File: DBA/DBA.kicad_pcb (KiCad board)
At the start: 2 copper layers, 45.7 x 61 mm, 1 part, among them U1 ESP32_NodeMCU_v1.1

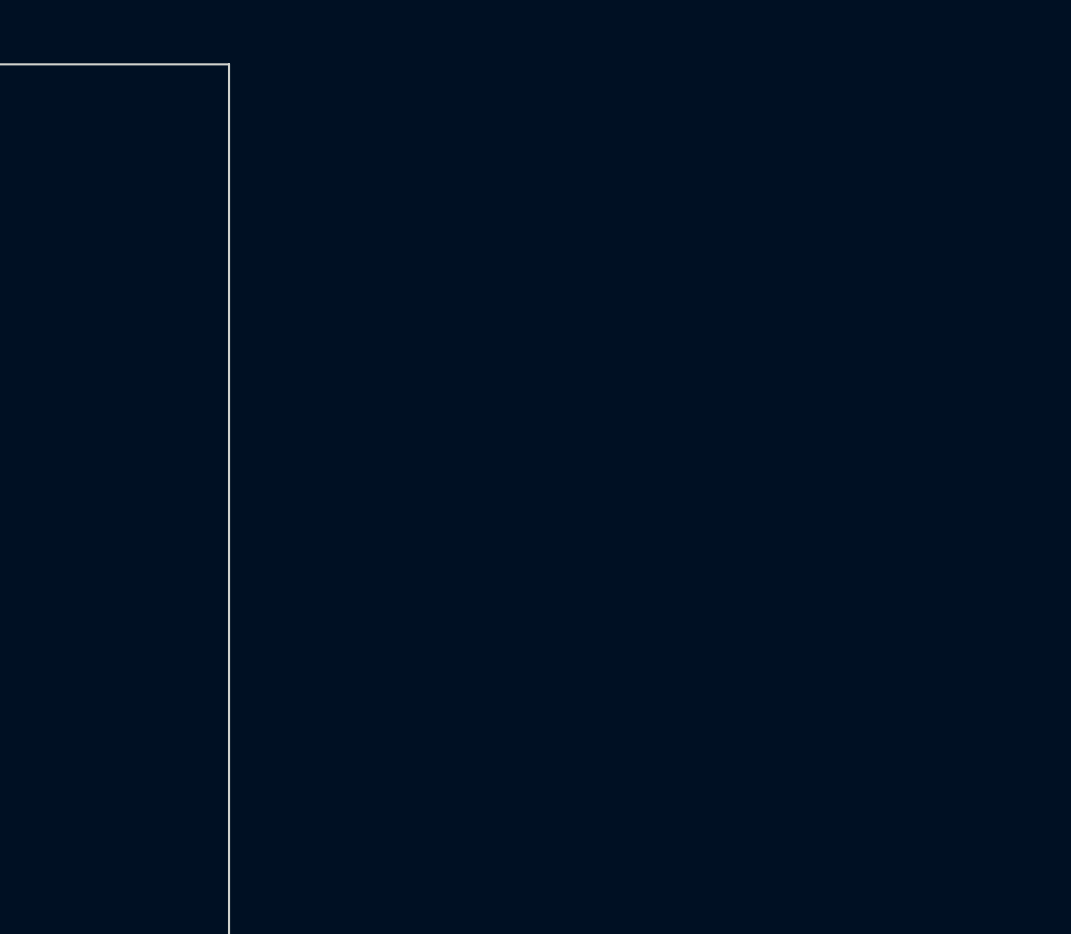
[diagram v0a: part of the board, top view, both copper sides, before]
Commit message: Created symbols for primary and secondary microphone
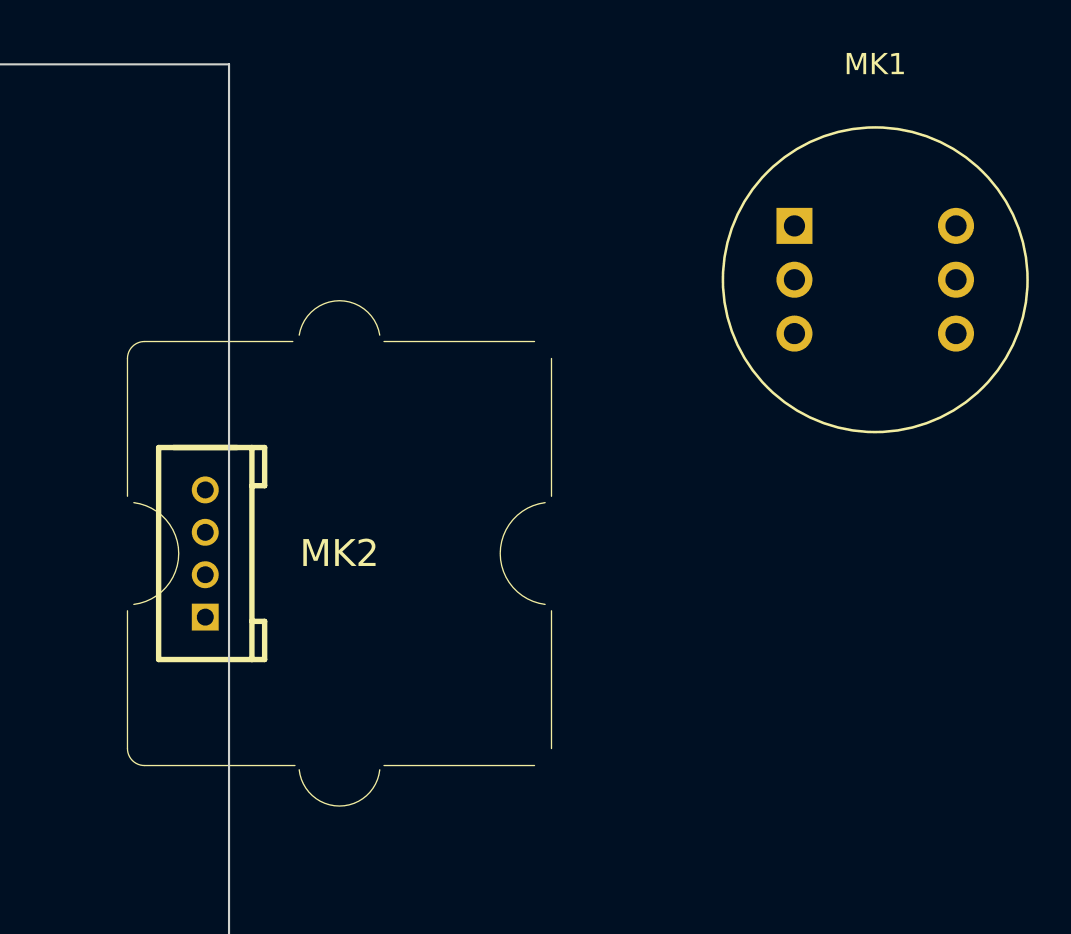
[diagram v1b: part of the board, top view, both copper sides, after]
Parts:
- added MK1: INMP441, Microphones:INMP441, F.Cu at (195.6, 71.1)
- added MK2: Grove, Microphones:Grove Sound Sensor, F.Cu at (170.3, 84.0)
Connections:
- U1 pad 1: unconnected-(U1-Pad1) -> Net-(MK1-Pad5)
- U1 pad 10: unconnected-(U1-Pad10) -> Net-(MK1-Pad4)
- U1 pad 14: unconnected-(U1-Pad14) -> GND
- U1 pad 32: unconnected-(U1-Pad32) -> GND
- U1 pad 36: unconnected-(U1-Pad36) -> Net-(MK1-Pad3)
- U1 pad 37: unconnected-(U1-Pad37) -> Net-(MK1-Pad2)
- U1 pad 38: unconnected-(U1-Pad38) -> GND
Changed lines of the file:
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@@
   (net 2 "unconnected-(U1-Pad8)")
   (net 3 "unconnected-(U1-Pad9)")
-  (net 4 "unconnected-(U1-Pad10)")
+  (net 4 "GND")
   (net 5 "unconnected-(U1-Pad11)")
   (net 6 "unconnected-(U1-Pad12)")
   (net 7 "unconnected-(U1-Pad13)")
-  (net 8 "unconnected-(U1-Pad14)")
+  (net 8 "Net-(MK1-Pad2)")
   (net 9 "unconnected-(U1-Pad15)")
   (net 10 "unconnected-(U1-Pad16)")
@@
   (net 22 "unconnected-(U1-Pad30)")
   (net 23 "unconnected-(U1-Pad31)")
-  (net 24 "unconnected-(U1-Pad32)")
+  (net 24 "Net-(MK1-Pad3)")
   (net 25 "unconnected-(U1-Pad33)")
   (net 26 "unconnected-(U1-Pad34)")
   (net 27 "unconnected-(U1-Pad35)")
-  (net 28 "unconnected-(U1-Pad36)")
-  (net 29 "unconnected-(U1-Pad38)")
-  (net 30 "unconnected-(U1-Pad1)")
+  (net 28 "Net-(MK1-Pad4)")
+  (net 29 "Net-(MK1-Pad5)")
+  (net 30 "unconnected-(MK2-Pad3)")
   (net 31 "unconnected-(U1-Pad2)")
   (net 32 "unconnected-(U1-Pad3)")
@@
   (net 36 "unconnected-(U1-Pad19)")
   (net 37 "unconnected-(U1-Pad26)")
-  (net 38 "unconnected-(U1-Pad37)")
+  (net 38 "unconnected-(MK2-Pad4)")
+  (footprint "Microphones:INMP441" (layer "F.Cu")
+    (at 195.58 71.12)
+    (descr "Through hole straight pin header, 2x03, 2.54mm pitch, double rows")
+    (tags "Through hole pin header THT 2x03 2.54mm double row")
+    (property "Sheetfile" "DBA.kicad_sch")
+    (property "Sheetname" "")
+    (attr through_hole)
+    (fp_text reference "MK1" (at 0 -10.16) (layer "F.SilkS")
+      (effects (font (size 1 1) (thickness 0.15)))
+    )
+    (fp_text value "INMP441" (at 1.27 4.87) (layer "F.Fab")
+      (effects (font (size 1 1) (thickness 0.15)))
+    )
+    (fp_text user "${REFERENCE}" (at -2.54 0 90) (layer "F.Fab")
+      (effects (font (size 1 1) (thickness 0.15)))
+    )
+    (fp_circle (center 0 0) (end 5.08 5.08) (layer "F.SilkS") (width 0.12) (fill none))
+    (fp_circle (center 0 0) (end 7.62 5.08) (layer "F.CrtYd") (width 0.05) (fill none))
+    (pad "1" thru_hole rect (at -3.81 -2.54) (size 1.7 1.7) (drill 1) (layers *.Cu *.Mask)
+      (net 4 "GND") (pinfunction "L/R") (pintype "input"))
+    (pad "2" thru_hole oval (at -3.81 0) (size 1.7 1.7) (drill 1) (layers *.Cu *.Mask)
+      (net 8 "Net-(MK1-Pad2)") (pinfunction "WS") (pintype "input"))
+    (pad "3" thru_hole oval (at -3.81 2.54) (size 1.7 1.7) (drill 1) (layers *.Cu *.Mask)
+      (net 24 "Net-(MK1-Pad3)") (pinfunction "SCK") (pintype "input"))
+    (pad "4" thru_hole oval (at 3.81 2.54) (size 1.7 1.7) (drill 1) (layers *.Cu *.Mask)
+      (net 28 "Net-(MK1-Pad4)") (pinfunction "SD") (pintype "input"))
+    (pad "5" thru_hole oval (at 3.81 0) (size 1.7 1.7) (drill 1) (layers *.Cu *.Mask)
+      (net 29 "Net-(MK1-Pad5)") (pinfunction "VDD") (pintype "power_in"))
+    (pad "6" thru_hole oval (at 3.81 -2.54) (size 1.7 1.7) (drill 1) (layers *.Cu *.Mask)
+      (net 4 "GND") (pinfunction "GND") (pintype "power_in"))
+    (model "${KICAD6_3DMODEL_DIR}/Connector_PinHeader_2.54mm.3dshapes/PinHeader_2x03_P2.54mm_Vertical.wrl"
+      (offset (xyz 0 0 0))
+      (scale (xyz 1 1 1))
+      (rotate (xyz 0 0 0))
+    )
+  )
   (footprint "Package_DIP:DIP-38_W22.86mm" (layer "F.Cu")
     (at 142.24 88.9)
@@
     (fp_line (start 10.485 -22.8) (end 10.485 26.73) (layer "F.Fab") (width 0.1))
     (pad "1" thru_hole rect (at -12.12 -21.53) (size 1.6 1.6) (drill 0.8) (layers *.Cu *.Mask)
-      (net 30 "unconnected-(U1-Pad1)") (pinfunction "3v3") (pintype "power_out"))
+      (net 29 "Net-(MK1-Pad5)") (pinfunction "3v3") (pintype "power_out"))
     (pad "2" thru_hole oval (at -12.12 -18.99) (size 1.6 1.6) (drill 0.8) (layers *.Cu *.Mask)
       (net 31 "unconnected-(U1-Pad2)") (pinfunction "En") (pintype "input"))
@@
       (net 3 "unconnected-(U1-Pad9)") (pinfunction "IO25") (pintype "input"))
     (pad "10" thru_hole oval (at -12.12 1.33) (size 1.6 1.6) (drill 0.8) (layers *.Cu *.Mask)
-      (net 4 "unconnected-(U1-Pad10)") (pinfunction "IO26") (pintype "input"))
+      (net 28 "Net-(MK1-Pad4)") (pinfunction "IO26") (pintype "input"))
     (pad "11" thru_hole oval (at -12.12 3.87) (size 1.6 1.6) (drill 0.8) (layers *.Cu *.Mask)
       (net 5 "unconnected-(U1-Pad11)") (pinfunction "IO27") (pintype "input"))
@@
       (net 7 "unconnected-(U1-Pad13)") (pinfunction "IO12") (pintype "input"))
     (pad "14" thru_hole oval (at -12.12 11.49) (size 1.6 1.6) (drill 0.8) (layers *.Cu *.Mask)
-      (net 8 "unconnected-(U1-Pad14)") (pinfunction "GND") (pintype "power_in"))
+      (net 4 "GND") (pinfunction "GND") (pintype "power_in"))
     (pad "15" thru_hole oval (at -12.12 14.03) (size 1.6 1.6) (drill 0.8) (layers *.Cu *.Mask)
       (net 9 "unconnected-(U1-Pad15)") (pinfunction "IO13") (pintype "input"))
@@
       (net 23 "unconnected-(U1-Pad31)") (pinfunction "IO19") (pintype "input"))
     (pad "32" thru_hole oval (at 10.74 -6.29) (size 1.6 1.6) (drill 0.8) (layers *.Cu *.Mask)
-      (net 24 "unconnected-(U1-Pad32)") (pinfunction "GND") (pintype "power_in"))
+      (net 4 "GND") (pinfunction "GND") (pintype "power_in"))
     (pad "33" thru_hole oval (at 10.74 -8.83) (size 1.6 1.6) (drill 0.8) (layers *.Cu *.Mask)
       (net 25 "unconnected-(U1-Pad33)") (pinfunction "IO21") (pintype "input"))
@@
       (net 27 "unconnected-(U1-Pad35)") (pinfunction "TxD0") (pintype "input"))
     (pad "36" thru_hole oval (at 10.74 -16.45) (size 1.6 1.6) (drill 0.8) (layers *.Cu *.Mask)
-      (net 28 "unconnected-(U1-Pad36)") (pinfunction "IO22") (pintype "input"))
+      (net 24 "Net-(MK1-Pad3)") (pinfunction "IO22") (pintype "input"))
     (pad "37" thru_hole oval (at 10.74 -18.99) (size 1.6 1.6) (drill 0.8) (layers *.Cu *.Mask)
-      (net 38 "unconnected-(U1-Pad37)") (pinfunction "IO23") (pintype "input"))
+      (net 8 "Net-(MK1-Pad2)") (pinfunction "IO23") (pintype "input"))
     (pad "38" thru_hole oval (at 10.74 -21.53) (size 1.6 1.6) (drill 0.8) (layers *.Cu *.Mask)
-      (net 29 "unconnected-(U1-Pad38)") (pinfunction "GND") (pintype "power_in"))
+      (net 4 "GND") (pinfunction "GND") (pintype "power_in"))
     (model "${KICAD6_3DMODEL_DIR}/Package_DIP.3dshapes/DIP-32_W15.24mm.wrl"
       (offset (xyz 0 0 0))
@@
     )
   )
+  (footprint "Microphones:Grove Sound Sensor" (layer "F.Cu")
+    (at 170.3096 84.033788)
+    (property "Sheetfile" "DBA.kicad_sch")
+    (property "Sheetname" "")
+    (fp_text reference "MK2" (at 0 0) (layer "F.SilkS")
+      (effects (font (size 1.27 1.27) (thickness 0.15)))
+    )
+    (fp_text value "Grove" (at 0 0) (layer "F.Fab") hide
+      (effects (font (size 1.27 1.27) (thickness 0.15)))
+    )
+    (fp_line (start -4.13 3.2) (end -4.13 -3.2) (layer "F.SilkS") (width 0.254))
+    (fp_line (start -7.33 5) (end -5.33 5) (layer "F.SilkS") (width 0.127))
+    (fp_line (start -9.2 -10) (end -2.2 -10) (layer "F.SilkS") (width 0.0254))
+    (fp_line (start -3.53 5) (end -3.53 3.2) (layer "F.SilkS") (width 0.254))
+    (fp_line (start -3.53 -3.2) (end -3.53 -5) (layer "F.SilkS") (width 0.254))
+    (fp_line (start -3.53 3.2) (end -4.13 3.2) (layer "F.SilkS") (width 0.254))
+    (fp_line (start -8.53 5) (end -4.13 5) (layer "F.SilkS") (width 0.254))
+    (fp_line (start 10 -2.7) (end 10 -9.2) (layer "F.SilkS") (width 0.0254))
+    (fp_line (start -3.53 -5) (end -4.13 -5) (layer "F.SilkS") (width 0.254))
+    (fp_line (start -9.2 10) (end -2.1 10) (layer "F.SilkS") (width 0.0254))
+    (fp_line (start -4.13 -3.2) (end -3.53 -3.2) (layer "F.SilkS") (width 0.254))
+    (fp_line (start 10 2.7) (end 10 9.2) (layer "F.SilkS") (width 0.0254))
+    (fp_line (start 9.2 -10) (end 2.1 -10) (layer "F.SilkS") (width 0.0254))
+    (fp_line (start -4.13 5) (end -3.53 5) (layer "F.SilkS") (width 0.254))
+    (fp_line (start -4.13 5) (end -4.13 3.2) (layer "F.SilkS") (width 0.254))
+    (fp_line (start -4.13 -3.2) (end -4.13 -5) (layer "F.SilkS") (width 0.254))
+    (fp_line (start -7.83 -5) (end -4.83 -5) (layer "F.SilkS") (width 0.254))
+    (fp_line (start 9.2 10) (end 2.1 10) (layer "F.SilkS") (width 0.0254))
+    (fp_line (start -4.13 -5) (end -8.53 -5) (layer "F.SilkS") (width 0.254))
+    (fp_line (start -8.53 5) (end -8.53 -5) (layer "F.SilkS") (width 0.254))
+    (fp_line (start -10 2.7) (end -10 9.2) (layer "F.SilkS") (width 0.0254))
+    (fp_line (start -10 -2.7) (end -10 -9.2) (layer "F.SilkS") (width 0.0254))
+    (fp_arc (start 1.9 10.2) (mid -0.000001 11.910767) (end -1.9 10.199998) (layer "F.SilkS") (width 0.0254))
+    (fp_arc (start -9.2 10) (mid -9.765685 9.765685) (end -10 9.2) (layer "F.SilkS") (width 0.0254))
+    (fp_arc (start -1.9 -10.3) (mid 0 -11.924188) (end 1.9 -10.3) (layer "F.SilkS") (width 0.0254))
+    (fp_arc (start -9.7 -2.4) (mid -7.582254 0) (end -9.7 2.4) (layer "F.SilkS") (width 0.0254))
+    (fp_arc (start 9.7 2.4) (mid 7.582254 0) (end 9.7 -2.4) (layer "F.SilkS") (width 0.0254))
+    (fp_arc (start -10 -9.2) (mid -9.765685 -9.765685) (end -9.2 -10) (layer "F.SilkS") (width 0.0254))
+    (pad "1" thru_hole rect (at -6.33 3 90) (size 1.27 1.27) (drill 0.8) (layers *.Cu *.Mask)
+      (net 4 "GND") (pinfunction "GND") (pintype "power_in") (solder_mask_margin 0.0508))
+    (pad "2" thru_hole circle (at -6.33 1 90) (size 1.27 1.27) (drill 0.8) (layers *.Cu *.Mask)
+      (net 29 "Net-(MK1-Pad5)") (pinfunction "VCC") (pintype "power_in") (solder_mask_margin 0.0508))
+    (pad "3" thru_hole circle (at -6.33 -1 90) (size 1.27 1.27) (drill 0.8) (layers *.Cu *.Mask)
+      (net 30 "unconnected-(MK2-Pad3)") (pinfunction "NC") (pintype "no_connect") (solder_mask_margin 0.0508))
+    (pad "4" thru_hole circle (at -6.33 -3 90) (size 1.27 1.27) (drill 0.8) (layers *.Cu *.Mask)
+      (net 38 "unconnected-(MK2-Pad4)") (pinfunction "SIG") (pintype "output") (solder_mask_margin 0.0508))
+  )
   (gr_rect (start 165.1 121.92) (end 119.38 60.96) (layer "Edge.Cuts") (width 0.1) (fill none))

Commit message: First complete model
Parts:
- added A1: TP4056, custom:TP4056Board, B.Cu at (119.4, 101.6)
- added BT1: Battery_Cell, Battery:BatteryHolder_Keystone_1042_1x18650, B.Cu at (160.0, 86.4)
- added C1: 100n, Capacitor_THT:C_Radial_D6.3mm_H5.0mm_P2.50mm, F.Cu at (166.4, 108.0)
- added C2: 100u, Capacitor_THT:CP_Radial_D5.0mm_P2.50mm, F.Cu at (157.5, 110.5)
- added J4: Conn_01x01_Male, Connector_PinHeader_2.54mm:PinHeader_1x01_P2.54mm_Vertical, F.Cu at (138.4, 109.2)
- added J5: Conn_01x01_Male, Connector_PinHeader_2.54mm:PinHeader_1x01_P2.54mm_Vertical, F.Cu at (151.1, 102.9)
- added U2: MCP1700-3302E_TO92, Package_TO_SOT_THT:TO-92_Inline, F.Cu at (147.3, 108.0)
- moved MK1 49.3 mm to (147.3, 81.3), turned to 90 degrees
- moved MK2 40.4 mm to (147.3, 50.8), turned to 90 degrees
- moved U1 30.6 mm to (119.4, 68.6), turned to 180 degrees
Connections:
- MK2 pad 4: unconnected-(MK2-Pad4) -> Net-(MK2-Pad4)
- U1 pad 9: unconnected-(U1-Pad9) -> Net-(MK2-Pad4)
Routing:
- net Net-(C1-Pad2): track 0.00 -> 76.2 mm, vias 0 -> 1
- net Net-(MK1-Pad3): track 0.00 -> 47.6 mm
- net Net-(MK1-Pad2): track 0.00 -> 45.0 mm, vias 0 -> 1
- net Net-(MK1-Pad4): track 0.00 -> 27.1 mm, vias 0 -> 1
- net Net-(MK2-Pad4): track 0.00 -> 21.2 mm
- net Net-(U2-Pad2): track 0.00 -> 8.89 mm
- added copper zone on B.Cu, net GND
- added copper zone on F.Cu, net GND
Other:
- board size 45.7 x 61 mm -> 68.6 x 94 mm
- board text added: "ECE496 Team 791 Kushagra Goel Rishabh Saini Kshitij Bhardwaj"

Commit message: first circular version{
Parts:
- A1: moved to F.Cu
- BT1: footprint Battery:BatteryHolder_Keystone_1042_1x18650 -> Battery:Battery_Custom
- moved C1 79.0 mm to (94.0, 76.2), turned to 0 degrees
- moved U2 57.5 mm to (94.0, 86.4), turned to 0 degrees
- moved C2 52.9 mm to (109.2, 132.1), turned to -90 degrees
- moved MK1 52.9 mm to (104.1, 111.8), turned to 180 degrees
- moved U1 47.1 mm to (132.8, 113.7), turned to 0 degrees
- moved J4 43.8 mm to (96.5, 96.5)
- moved BT1 40.6 mm to (130.6, 58.4), turned to 180 degrees
- moved A1 38.2 mm to (157.5, 104.1)
- moved J5 32.0 mm to (147.3, 134.6)
- moved MK2 28.4 mm to (142.2, 78.7), turned to 0 degrees
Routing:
- net Net-(C1-Pad2): track 76.2 -> 0.00 mm, vias 1 -> 0
- net Net-(MK1-Pad3): track 47.6 -> 0.00 mm
- net Net-(MK1-Pad2): track 45.0 -> 0.00 mm, vias 1 -> 0
- net Net-(MK1-Pad4): track 27.1 -> 0.00 mm, vias 1 -> 0
- net Net-(MK2-Pad4): track 21.2 -> 0.00 mm
- net Net-(J4-Pad1): track 8.89 -> 0.00 mm
- removed copper zone on B.Cu, net GND
- removed copper zone on F.Cu, net GND
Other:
- board size 68.6 x 94 mm -> 101.6 x 101.6 mm
- board text removed: "ECE496 Team 791 Kushagra Goel Rishabh Saini Kshitij Bhardwaj"

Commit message: Final circular design
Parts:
- A1: moved to B.Cu
- moved MK1 62.5 mm to (160.0, 83.8), turned to 90 degrees
- moved J5 50.9 mm to (144.8, 83.8)
- moved A1 43.8 mm to (135.9, 66.0), turned to -90 degrees
- moved BT1 33.4 mm to (135.4, 91.4), turned to 0 degrees
- moved J4 30.7 mm to (124.5, 83.8)
- moved MK2 30.6 mm to (111.8, 76.2), turned to 90 degrees
- moved C1 27.3 mm to (104.1, 101.6)
- moved C2 15.4 mm to (106.7, 116.8), turned to 180 degrees
- moved U2 12.7 mm to (104.1, 94.0)
- moved U1 2.70 mm to (134.6, 111.8), turned to 90 degrees
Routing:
- net Net-(C1-Pad2): track 0.00 -> 102.3 mm
- net Net-(MK1-Pad4): track 0.00 -> 72.7 mm
- net Net-(MK1-Pad2): track 0.00 -> 49.9 mm
- net Net-(MK1-Pad3): track 0.00 -> 49.9 mm
- net Net-(MK2-Pad4): track 0.00 -> 33.4 mm
- net Net-(J4-Pad1): track 0.00 -> 24.0 mm
- net GND: track 0.00 -> 7.62 mm
- added copper zone on F.Cu, net GND
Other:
- board size 101.6 x 101.6 mm -> 83.8 x 83.8 mm

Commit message: Added gerber files
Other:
- board text added: "ECE496 Team 791 Deep Bio-Acoustics"
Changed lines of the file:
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@@
     (pad_to_mask_clearance 0)
     (pcbplotparams
-      (layerselection 0x00010fc_ffffffff)
+      (layerselection 0x00010f0_ffffffff)
       (disableapertmacros false)
       (usegerberextensions false)
-      (usegerberattributes true)
+      (usegerberattributes false)
       (usegerberadvancedattributes true)
       (creategerberjobfile true)
@@
       (outputformat 1)
       (mirror false)
-      (drillshape 1)
+      (drillshape 0)
       (scaleselection 1)
       (outputdirectory "")
@@
     (property "Sheetname" "")
     (attr smd)
-    (fp_text reference "BT1" (at 0 11.5) (layer "B.SilkS")
+    (fp_text reference "BT1" (at 0 2.54) (layer "B.SilkS")
       (effects (font (size 1 1) (thickness 0.15)) (justify mirror))
     )
@@
   )
   (gr_circle (center 133.35 93.98) (end 175.26 93.98) (layer "Edge.Cuts") (width 0.1) (fill none))
+  (gr_text "ECE496\nTeam 791\nDeep Bio-Acoustics" (at 134.62 111.76) (layer "B.SilkS")
+    (effects (font (size 1.778 1.778) (thickness 0.3)) (justify mirror))
+  )
   (segment (start 157.48 80.01) (end 157.48 87.63) (width 0.25) (layer "B.Cu") (net 4))
   (segment (start 149.86 97.79) (end 118.86 97.79) (width 0.25) (layer "F.Cu") (net 8))
